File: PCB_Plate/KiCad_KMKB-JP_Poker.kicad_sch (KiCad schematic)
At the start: 21 parts, among them SW1 SW_Push, U1 ATmega32U4-MU, U2 PRTR5V0U2X, Y1 16MHz

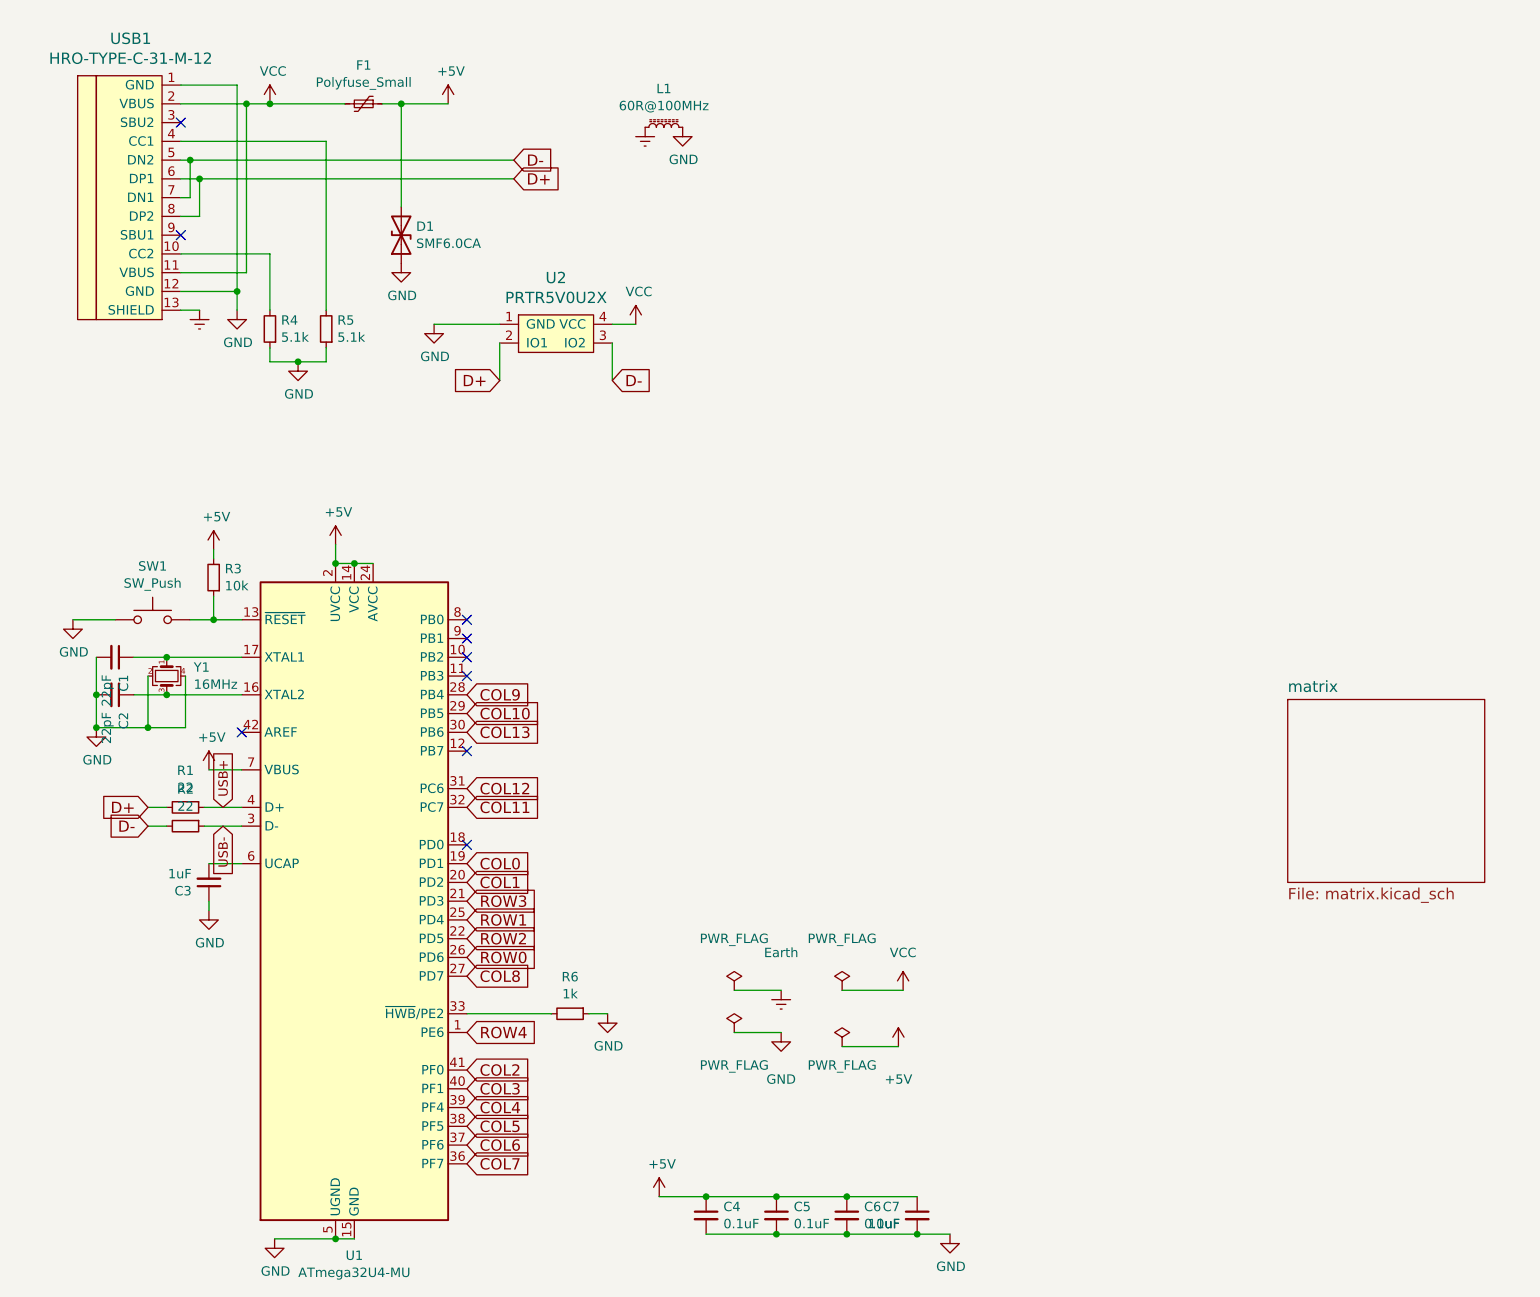
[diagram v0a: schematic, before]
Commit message: ドーターボード用の配線穴を設置
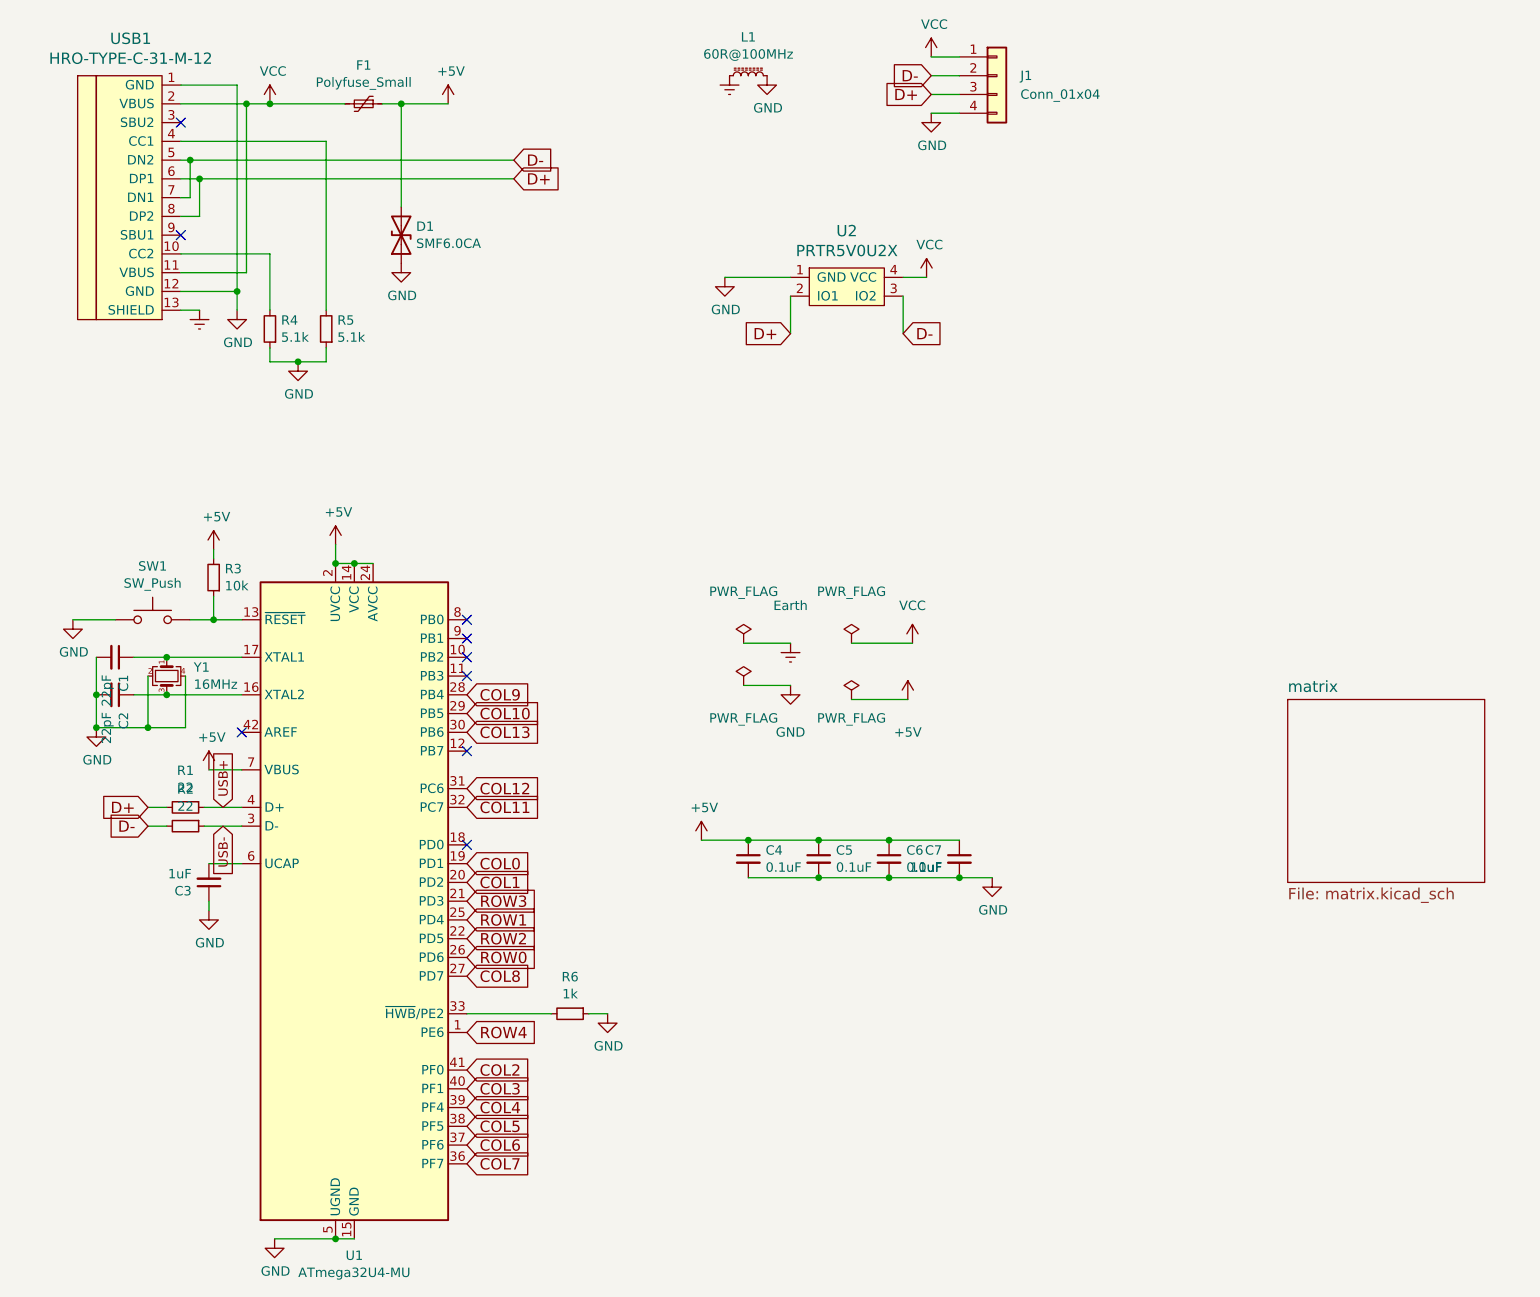
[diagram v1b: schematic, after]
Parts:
- added J1: Conn_01x04, Connector_PinHeader_2.54mm:PinHeader_1x04_P2.54mm_Vertical, symbol Connector_Generic:Conn_01x04
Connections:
- net D+: now also J1.3 (Pin_3)
- net D-: now also J1.2 (Pin_2)
- net GND: now also J1.4 (Pin_4)
- net VCC: now also J1.1 (Pin_1)
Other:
- moved on the sheet: C4, C5, C6, C7, L1, U2
